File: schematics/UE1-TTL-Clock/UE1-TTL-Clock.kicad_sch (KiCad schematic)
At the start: 6 parts, among them J1 Edge 1, J2 Edge 2

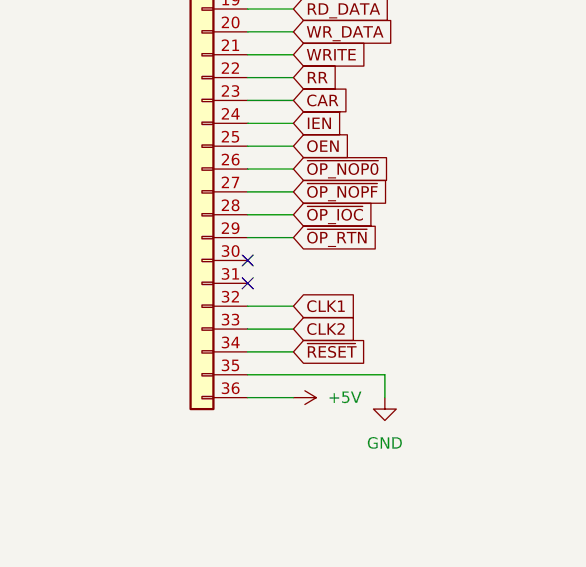
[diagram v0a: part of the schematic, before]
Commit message: Lay out clock board
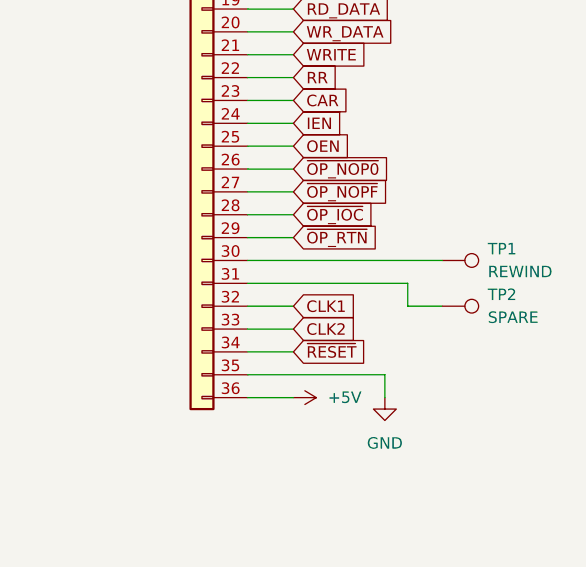
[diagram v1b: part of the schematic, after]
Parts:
- added TP1: REWIND, TestPoint:TestPoint_Pad_D1.5mm, symbol Connector:TestPoint
- added TP2: SPARE, TestPoint:TestPoint_Pad_D1.5mm, symbol Connector:TestPoint
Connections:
- net at J2.30 (Pin_30): now also TP1.1
- net at J2.31 (Pin_31): now also TP2.1
- no-connect marks 2 -> 0
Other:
- title: UE1- TTL Clock and Diagnostics -> UE1-TTL Clock and Front Panel
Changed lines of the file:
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@@
 	(paper "A4")
 	(title_block
-		(title "UE1- TTL Clock and Diagnostics")
+		(title "UE1-TTL Clock and Front Panel")
 		(date "2025")
 		(rev "1")
@@
 		(comment 3 "Edge Connectors")
 	)
-	(no_connect
-		(at 176.53 142.24)
-	)
-	(no_connect
-		(at 176.53 139.7)
-	)
 	(wire
 		(pts
@@
 	(wire
 		(pts
+			(xy 176.53 142.24) (xy 194.31 142.24)
+		)
+		(stroke
+			(width 0)
+			(type default)
+		)
+	)
+	(wire
+		(pts
 			(xy 176.53 106.68) (xy 181.61 106.68)
 		)
@@
 	(wire
 		(pts
+			(xy 194.31 142.24) (xy 194.31 144.78)
+		)
+		(stroke
+			(width 0)
+			(type default)
+		)
+	)
+	(wire
+		(pts
 			(xy 176.53 76.2) (xy 181.61 76.2)
 		)
@@
 	(wire
 		(pts
+			(xy 194.31 144.78) (xy 198.12 144.78)
+		)
+		(stroke
+			(width 0)
+			(type default)
+		)
+	)
+	(wire
+		(pts
 			(xy 104.14 144.78) (xy 109.22 144.78)
 		)
@@
 		(pts
 			(xy 176.53 111.76) (xy 181.61 111.76)
+		)
+		(stroke
+			(width 0)
+			(type default)
+		)
+	)
+	(wire
+		(pts
+			(xy 176.53 139.7) (xy 198.12 139.7)
 		)
 		(stroke
@@
 	)
 	(symbol
+		(lib_id "Connector:TestPoint")
+		(at 198.12 139.7 270)
+		(unit 1)
+		(exclude_from_sim no)
+		(in_bom yes)
+		(on_board yes)
+		(dnp no)
+		(fields_autoplaced yes)
+		(property "Reference" "TP1"
+			(at 203.2 138.4299 90)
+			(effects
+				(font
+					(size 1.27 1.27)
+				)
+				(justify left)
+			)
+		)
+		(property "Value" "REWIND"
+			(at 203.2 140.9699 90)
+			(effects
+				(font
+					(size 1.27 1.27)
+				)
+				(justify left)
+			)
+		)
+		(property "Footprint" "TestPoint:TestPoint_Pad_D1.5mm"
+			(at 198.12 144.78 0)
+			(effects
+				(font
+					(size 1.27 1.27)
+				)
+				(hide yes)
+			)
+		)
+		(property "Datasheet" "~"
+			(at 198.12 144.78 0)
+			(effects
+				(font
+					(size 1.27 1.27)
+				)
+				(hide yes)
+			)
+		)
+		(property "Description" "test point"
+			(at 198.12 139.7 0)
+			(effects
+				(font
+					(size 1.27 1.27)
+				)
+				(hide yes)
+			)
+		)
+		(pin "1"
+		)
+		(instances
+			(project ""
+				(path "/3387ba40-0694-43b2-a156-d12ce9552f1f"
+					(reference "TP1")
+					(unit 1)
+				)
+			)
+		)
+	)
+	(symbol
 		(lib_id "Mechanical:MountingHole")
 		(at 45.72 173.99 0)
@@
 					(unit 1)
 				)
+			)
+		)
+	)
+	(symbol
+		(lib_id "Connector:TestPoint")
+		(at 198.12 144.78 270)
+		(unit 1)
+		(exclude_from_sim no)
+		(in_bom yes)
+		(on_board yes)
+		(dnp no)
+		(fields_autoplaced yes)
+		(property "Reference" "TP2"
+			(at 203.2 143.5099 90)
+			(effects
+				(font
+					(size 1.27 1.27)
+				)
+				(justify left)
+			)
+		)
+		(property "Value" "SPARE"
+			(at 203.2 146.0499 90)
+			(effects
+				(font
+					(size 1.27 1.27)
+				)
+				(justify left)
+			)
+		)
+		(property "Footprint" "TestPoint:TestPoint_Pad_D1.5mm"
+			(at 198.12 149.86 0)
+			(effects
+				(font
+					(size 1.27 1.27)
+				)
+				(hide yes)
+			)
+		)
+		(property "Datasheet" "~"
+			(at 198.12 149.86 0)
+			(effects
+				(font
+					(size 1.27 1.27)
+				)
+				(hide yes)
+			)
+		)
+		(property "Description" "test point"
+			(at 198.12 144.78 0)
+			(effects
+				(font
+					(size 1.27 1.27)
+				)
+				(hide yes)
+			)
+		)
+		(pin "1"
+		)
+		(instances
+			(project "UE1-TTL-Clock"
+				(path "/3387ba40-0694-43b2-a156-d12ce9552f1f"
+					(reference "TP2")
+					(unit 1)
+				)
